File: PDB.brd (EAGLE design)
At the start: 146 x 125.4 mm, 64 parts, among them IC1 LM555N

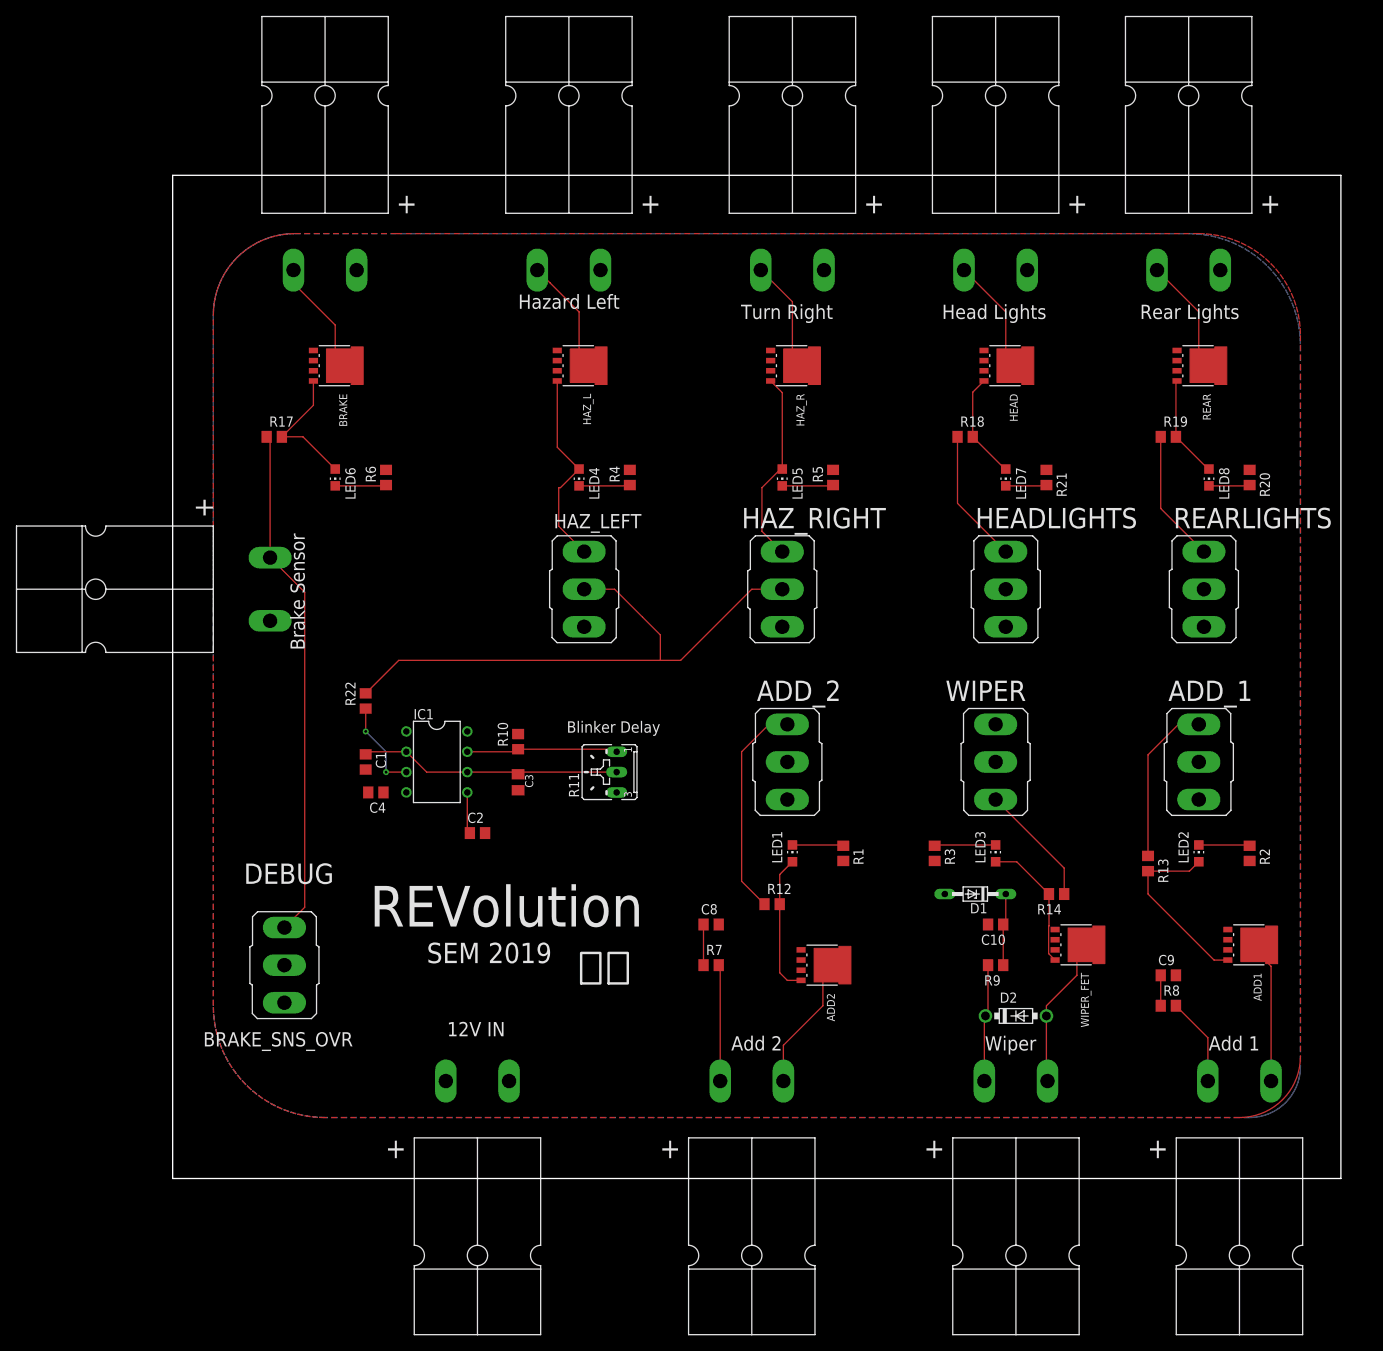
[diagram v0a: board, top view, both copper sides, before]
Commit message: wide traces
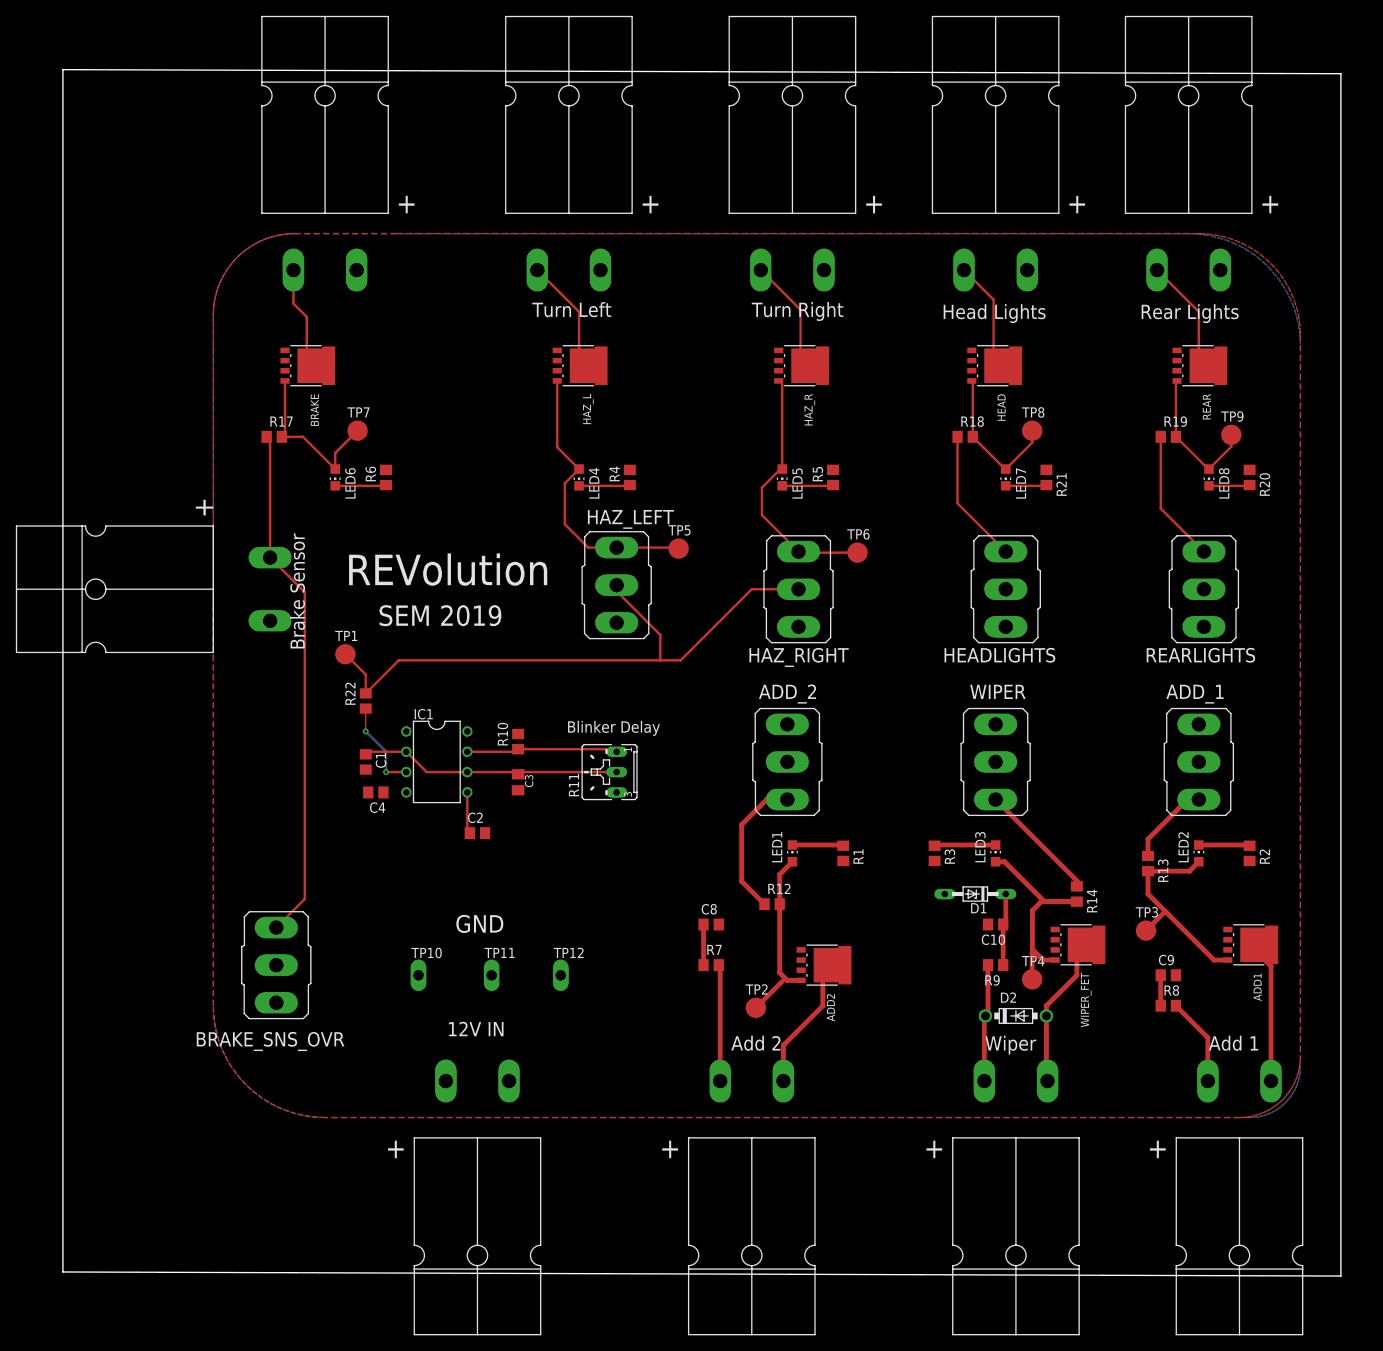
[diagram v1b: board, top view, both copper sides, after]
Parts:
- added TP1, TP2, TP3, TP4, TP5, TP6, TP7, TP8, TP9: PTR1B2,54, testpad:B2,54
- added TP10, TP11, TP12: PTR1PAD1-13Y, testpad:P1-13Y
- moved HAZ_LEFT 4.10 mm to (66.9, 64.0)
- moved BRAKE 3.56 mm to (28.2, 91.4)
- moved R14 2.54 mm to (124.5, 25.4), turned to 270 degrees
- moved HAZ_RIGHT 2.03 mm to (89.7, 63.5)
- moved HEAD 1.52 mm to (114.0, 91.4)
- moved BRAKE_SNS_OVR 1.02 mm to (24.4, 16.5)
- moved HAZ_R 1.02 mm to (89.9, 91.4)
- turned ADD_1 to 180 degrees
- turned ADD_2 to 180 degrees
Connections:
- net 555_OUT: now also TP1.TP
- net GND: now also TP10.TP, TP11.TP, TP12.TP
- net H2: now also TP6.TP
- net H3: now also TP5.TP
- net N$13: now also TP7.TP
- net N$14: now also TP8.TP
- net N$15: now also TP9.TP
- net N$22: now also TP4.TP
- net N$26: now also TP3.TP
- net N$7: now also TP2.TP
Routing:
- net N$22: track 16.9 -> 30.2 mm
- net H3: track 25.0 -> 35.3 mm
- net H5: track 20.6 -> 11.0 mm
- net H6: track 27.4 -> 18.1 mm
- net H2: track 24.3 -> 32.1 mm
- net N$7: track 17.6 -> 23.6 mm
- net N$14: track 13.4 -> 19.0 mm
- net N$15: track 12.8 -> 18.3 mm
- net 555_OUT: track 72.5 -> 77.1 mm
- net N$13: track 17.0 -> 21.4 mm
- net N$26: track 23.1 -> 26.5 mm
- net N$25: track 14.1 -> 12.6 mm
- net N$1: track 14.1 -> 13.5 mm
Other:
- board size 146 x 125.4 mm -> 159.7 x 150.8 mm
- board text added: "GND"
- board text added: "Turn Left"
- board text removed: "DEBUG"
- board text removed: "Hazard Left"
- board text removed: "大陆"

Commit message: wide traces
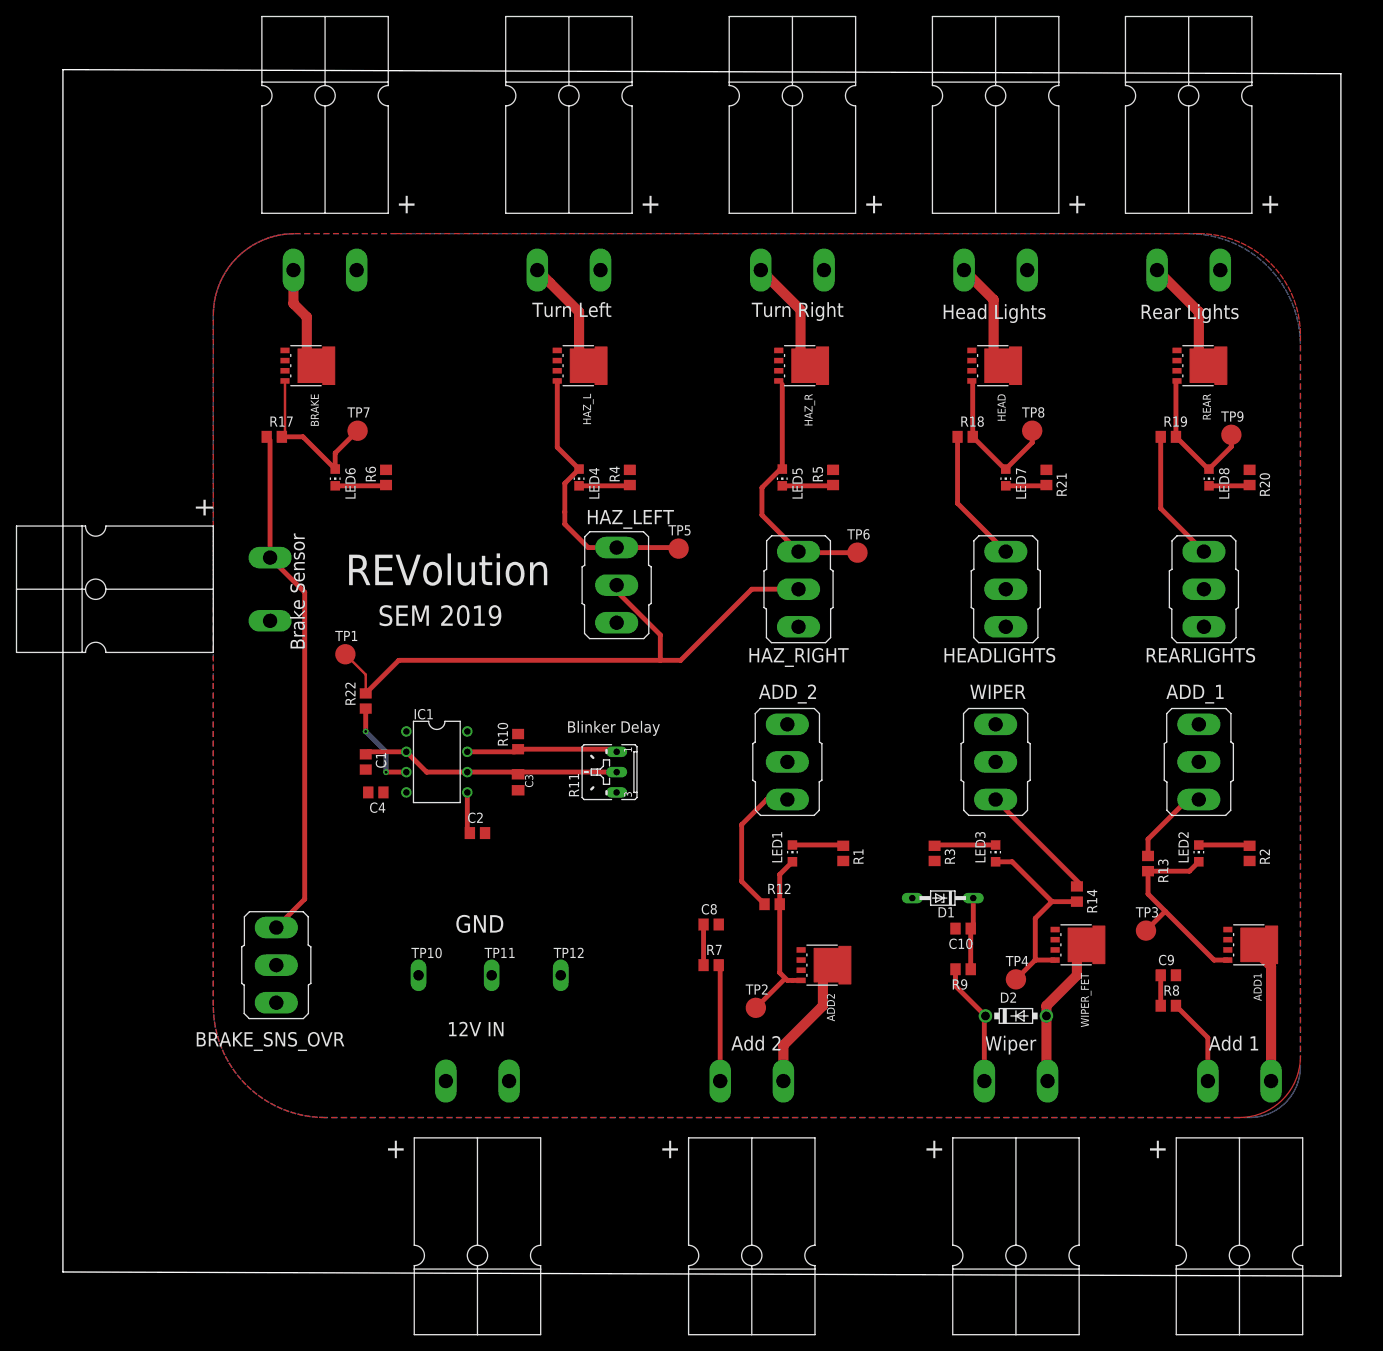
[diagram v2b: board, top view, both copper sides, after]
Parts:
- moved D1 4.10 mm to (107.7, 24.9)
- moved R9 4.10 mm to (110.2, 16.0)
- moved C10 4.10 mm to (110.2, 21.1)
- moved TP4 2.03 mm to (116.8, 14.7)
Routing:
- net N$22: track 30.2 -> 26.3 mm
- net N$20: track 14.7 -> 15.6 mm

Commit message: added stuff to pdb
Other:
- board size 159.7 x 150.8 mm -> 159.7 x 151.3 mm
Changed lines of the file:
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@@
 <board>
 <plain>
-<wire x1="-2.286" y1="-21.844" x2="157.46" y2="-22.352" width="0" layer="20"/>
-<wire x1="157.46" y1="-22.352" x2="157.46" y2="127.94" width="0" layer="20"/>
-<wire x1="157.46" y1="127.94" x2="-2.286" y2="128.448" width="0" layer="20"/>
-<wire x1="-2.286" y1="128.448" x2="-2.286" y2="-21.844" width="0" layer="20"/>
+<wire x1="-2.286" y1="-22.86" x2="157.46" y2="-22.86" width="0" layer="20"/>
+<wire x1="157.46" y1="-22.86" x2="157.46" y2="128.448" width="0" layer="20"/>
+<wire x1="157.46" y1="128.448" x2="-2.286" y2="128.448" width="0" layer="20"/>
+<wire x1="-2.286" y1="128.448" x2="-2.286" y2="-22.86" width="0" layer="20"/>
 <text x="46.736" y="20.574" size="2.1844" layer="25">GND</text>
 <text x="45.72" y="7.62" size="1.778" layer="25">12V IN </text>
